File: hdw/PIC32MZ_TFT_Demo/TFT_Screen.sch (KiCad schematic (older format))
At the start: 24 parts, among them J1101 TFT FFC, U1101 SiP32431DR3

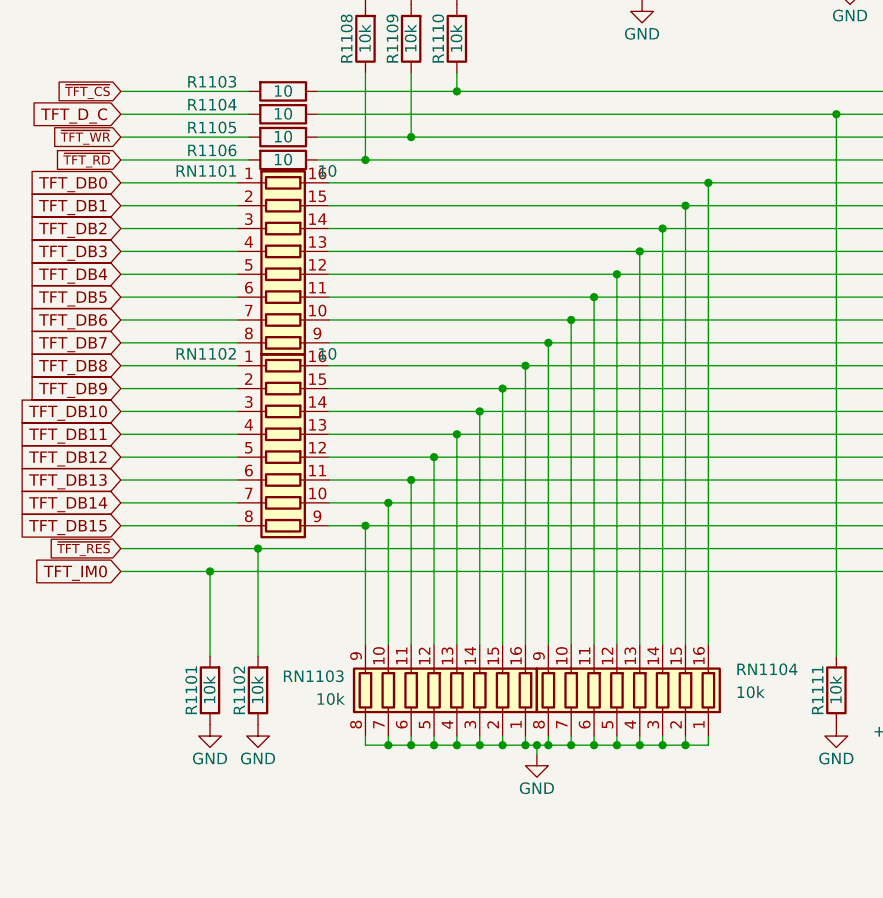
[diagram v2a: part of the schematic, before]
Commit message: More board part arrangement
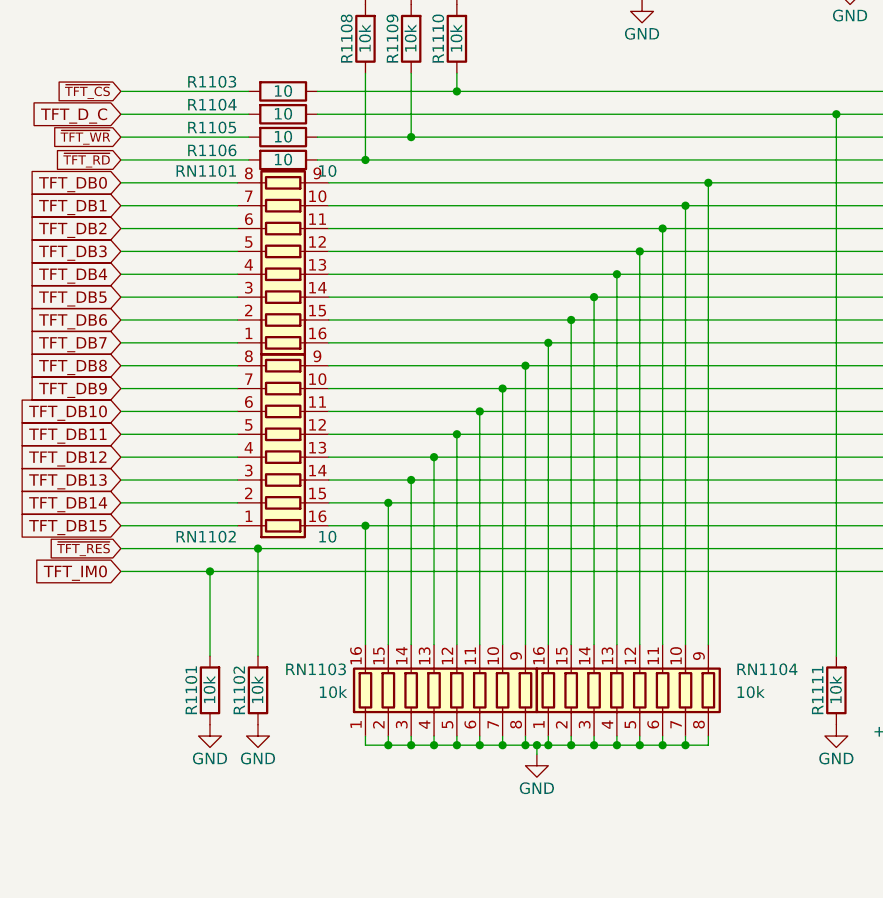
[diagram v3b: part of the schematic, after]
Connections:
- net TFT_DB0: now also RN1101.8 (R8.1); no longer RN1101.1 (R1.1)
- net TFT_DB1: now also RN1101.7 (R7.1); no longer RN1101.2 (R2.1)
- net TFT_DB10: now also RN1102.6 (R6.1); no longer RN1102.3 (R3.1)
- net TFT_DB11: now also RN1102.5 (R5.1); no longer RN1102.4 (R4.1)
- net TFT_DB12: now also RN1102.4 (R4.1); no longer RN1102.5 (R5.1)
- net TFT_DB13: now also RN1102.3 (R3.1); no longer RN1102.6 (R6.1)
- net TFT_DB14: now also RN1102.2 (R2.1); no longer RN1102.7 (R7.1)
- net TFT_DB15: now also RN1102.1 (R1.1); no longer RN1102.8 (R8.1)
- net TFT_DB2: now also RN1101.6 (R6.1); no longer RN1101.3 (R3.1)
- net TFT_DB3: now also RN1101.5 (R5.1); no longer RN1101.4 (R4.1)
- net TFT_DB4: now also RN1101.4 (R4.1); no longer RN1101.5 (R5.1)
- net TFT_DB5: now also RN1101.3 (R3.1); no longer RN1101.6 (R6.1)
- net TFT_DB6: now also RN1101.2 (R2.1); no longer RN1101.7 (R7.1)
- net TFT_DB7: now also RN1101.1 (R1.1); no longer RN1101.8 (R8.1)
- net TFT_DB8: now also RN1102.8 (R8.1); no longer RN1102.1 (R1.1)
- net TFT_DB9: now also RN1102.7 (R7.1); no longer RN1102.2 (R2.1)
- net at RN1101.16 (R1.2), RN1104.16 (R1.2): now also J1101.21 (Pin_21); no longer J1101.14 (Pin_14)
- net at RN1101.15 (R2.2), RN1104.15 (R2.2): now also J1101.20 (Pin_20); no longer J1101.15 (Pin_15)
- net at RN1101.14 (R3.2), RN1104.14 (R3.2): now also J1101.19 (Pin_19); no longer J1101.16 (Pin_16)
- net at RN1101.13 (R4.2), RN1104.13 (R4.2): now also J1101.18 (Pin_18); no longer J1101.17 (Pin_17)
- net at RN1101.12 (R5.2), RN1104.12 (R5.2): now also J1101.17 (Pin_17); no longer J1101.18 (Pin_18)
- net at RN1101.11 (R6.2), RN1104.11 (R6.2): now also J1101.16 (Pin_16); no longer J1101.19 (Pin_19)
- net at RN1101.10 (R7.2), RN1104.10 (R7.2): now also J1101.15 (Pin_15); no longer J1101.20 (Pin_20)
- net at RN1101.9 (R8.2), RN1104.9 (R8.2): now also J1101.14 (Pin_14); no longer J1101.21 (Pin_21)
- net at RN1102.16 (R1.2), RN1103.16 (R1.2): now also J1101.29 (Pin_29); no longer J1101.22 (Pin_22)
- net at RN1102.15 (R2.2), RN1103.15 (R2.2): now also J1101.28 (Pin_28); no longer J1101.23 (Pin_23)
- net at RN1102.14 (R3.2), RN1103.14 (R3.2): now also J1101.27 (Pin_27); no longer J1101.24 (Pin_24)
- net at RN1102.13 (R4.2), RN1103.13 (R4.2): now also J1101.26 (Pin_26); no longer J1101.25 (Pin_25)
- net at RN1102.12 (R5.2), RN1103.12 (R5.2): now also J1101.25 (Pin_25); no longer J1101.26 (Pin_26)
- net at RN1102.11 (R6.2), RN1103.11 (R6.2): now also J1101.24 (Pin_24); no longer J1101.27 (Pin_27)
- net at RN1102.10 (R7.2), RN1103.10 (R7.2): now also J1101.23 (Pin_23); no longer J1101.28 (Pin_28)
- net at RN1102.9 (R8.2), RN1103.9 (R8.2): now also J1101.22 (Pin_22); no longer J1101.29 (Pin_29)
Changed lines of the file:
@@
 NoConn ~ 6260 5320
-$Comp
-L Device:R_Pack08 RN1103
-U 1 1 5EE9C32C
-P 3830 4940
-F 0 "RN1103" H 4220 5000 50  0000 L CNN
-F 1 "10k" H 4220 4900 50  0000 L CNN
-F 2 "Resistors_SMD:R_Array_Convex_8x0602" V 4305 4940 50  0001 C CNN
-F 3 "~" H 3830 4940 50  0001 C CNN
-F 4 "Y1103CT-ND" H 3830 4940 50  0001 C CNN "Digi-Key PN"
-	1    3830 4940
-	-1   0    0    -1
-$EndComp
 $Comp
 L power:GND #PWR01110
@@
 	1    0    0    -1
 $EndComp
-Wire Wire Line
-	2460 4320 3060 4320
 $Comp
 L Custom_Library:R_Custom R?
@@
 	3060 4790 3060 4320
 Connection ~ 3060 4320
-Wire Wire Line
-	3060 4320 6260 4320
 $Comp
 L Custom_Library:R_Custom R?
@@
 L Device:R_Pack08 RN1104
 U 1 1 5EF819E2
-P 4630 4940
-F 0 "RN1104" H 4110 5030 50  0000 R CNN
-F 1 "10k" H 4110 4930 50  0000 R CNN
-F 2 "Resistors_SMD:R_Array_Convex_8x0602" V 5105 4940 50  0001 C CNN
-F 3 "~" H 4630 4940 50  0001 C CNN
-F 4 "Y1103CT-ND" H 4630 4940 50  0001 C CNN "Digi-Key PN"
-	1    4630 4940
-	-1   0    0    -1
-$EndComp
-$Comp
-L Device:R_Pack08 RN1101
-U 1 1 5EF88E7C
-P 3170 3120
-F 0 "RN1101" V 2720 2920 50  0000 R CNN
-F 1 "10" V 2720 3270 50  0000 L CNN
-F 2 "Resistors_SMD:R_Array_Convex_8x0602" V 3645 3120 50  0001 C CNN
-F 3 "~" H 3170 3120 50  0001 C CNN
-F 4 "Y1100CT-ND" H 3170 3120 50  0001 C CNN "Digi-Key PN"
-	1    3170 3120
-	0    1    1    0
+P 4730 4940
+F 0 "RN1104" H 5150 5030 50  0000 L CNN
+F 1 "10k" H 5150 4930 50  0000 L CNN
+F 2 "Resistors_SMD:R_Array_Convex_8x0602" V 5205 4940 50  0001 C CNN
+F 3 "~" H 4730 4940 50  0001 C CNN
+F 4 "Y1103CT-ND" H 4730 4940 50  0001 C CNN "Digi-Key PN"
+	1    4730 4940
+	1    0    0    -1
 $EndComp
 $Comp
 L Device:R_Pack08 RN1102
 U 1 1 5EF8BB30
-P 3170 3920
-F 0 "RN1102" V 2720 3720 50  0000 R CNN
-F 1 "10" V 2720 4070 50  0000 L CNN
-F 2 "Resistors_SMD:R_Array_Convex_8x0602" V 3645 3920 50  0001 C CNN
-F 3 "~" H 3170 3920 50  0001 C CNN
-F 4 "Y1100CT-ND" H 3170 3920 50  0001 C CNN "Digi-Key PN"
-	1    3170 3920
-	0    1    1    0
+P 3170 3820
+F 0 "RN1102" V 2720 3620 50  0000 R CNN
+F 1 "10" V 2720 3970 50  0000 L CNN
+F 2 "Resistors_SMD:R_Array_Convex_8x0602" V 3645 3820 50  0001 C CNN
+F 3 "~" H 3170 3820 50  0001 C CNN
+F 4 "Y1100CT-ND" H 3170 3820 50  0001 C CNN "Digi-Key PN"
+	1    3170 3820
+	0    1    -1   0
 $EndComp
 $Comp
@@
 Wire Wire Line
 	5010 6510 4470 6510
+$Comp
+L Device:R_Pack08 RN1103
+U 1 1 5EE9C32C
+P 3930 4940
+F 0 "RN1103" H 3450 5030 50  0000 R CNN
+F 1 "10k" H 3450 4930 50  0000 R CNN
+F 2 "Resistors_SMD:R_Array_Convex_8x0602" V 4405 4940 50  0001 C CNN
+F 3 "~" H 3930 4940 50  0001 C CNN
+F 4 "Y1103CT-ND" H 3930 4940 50  0001 C CNN "Digi-Key PN"
+	1    3930 4940
+	1    0    0    -1
+$EndComp
+$Comp
+L Device:R_Pack08 RN1101
+U 1 1 5EF88E7C
+P 3170 3020
+F 0 "RN1101" V 3520 2820 50  0000 R CNN
+F 1 "10" V 3520 3170 50  0000 L CNN
+F 2 "Resistors_SMD:R_Array_Convex_8x0602" V 3645 3020 50  0001 C CNN
+F 3 "~" H 3170 3020 50  0001 C CNN
+F 4 "Y1100CT-ND" H 3170 3020 50  0001 C CNN "Digi-Key PN"
+	1    3170 3020
+	0    1    -1   0
+$EndComp
+Wire Wire Line
+	2460 4320 3060 4320
+Wire Wire Line
+	3060 4320 6260 4320
 $EndSCHEMATC
